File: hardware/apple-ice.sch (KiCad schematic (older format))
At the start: 80 parts, among them J1 TO_SP_DRIVE, J2 USB_B_Micro, J3 SPI_FLASH_PROG, P1 A2Bus-apple2, SW1 SW_Push, SW2 SW_Push, SW3 SW_Push, U1 SN74LVC8T245PW, U10 W25Q16JVSS, U2 SN74LVC8T245PW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

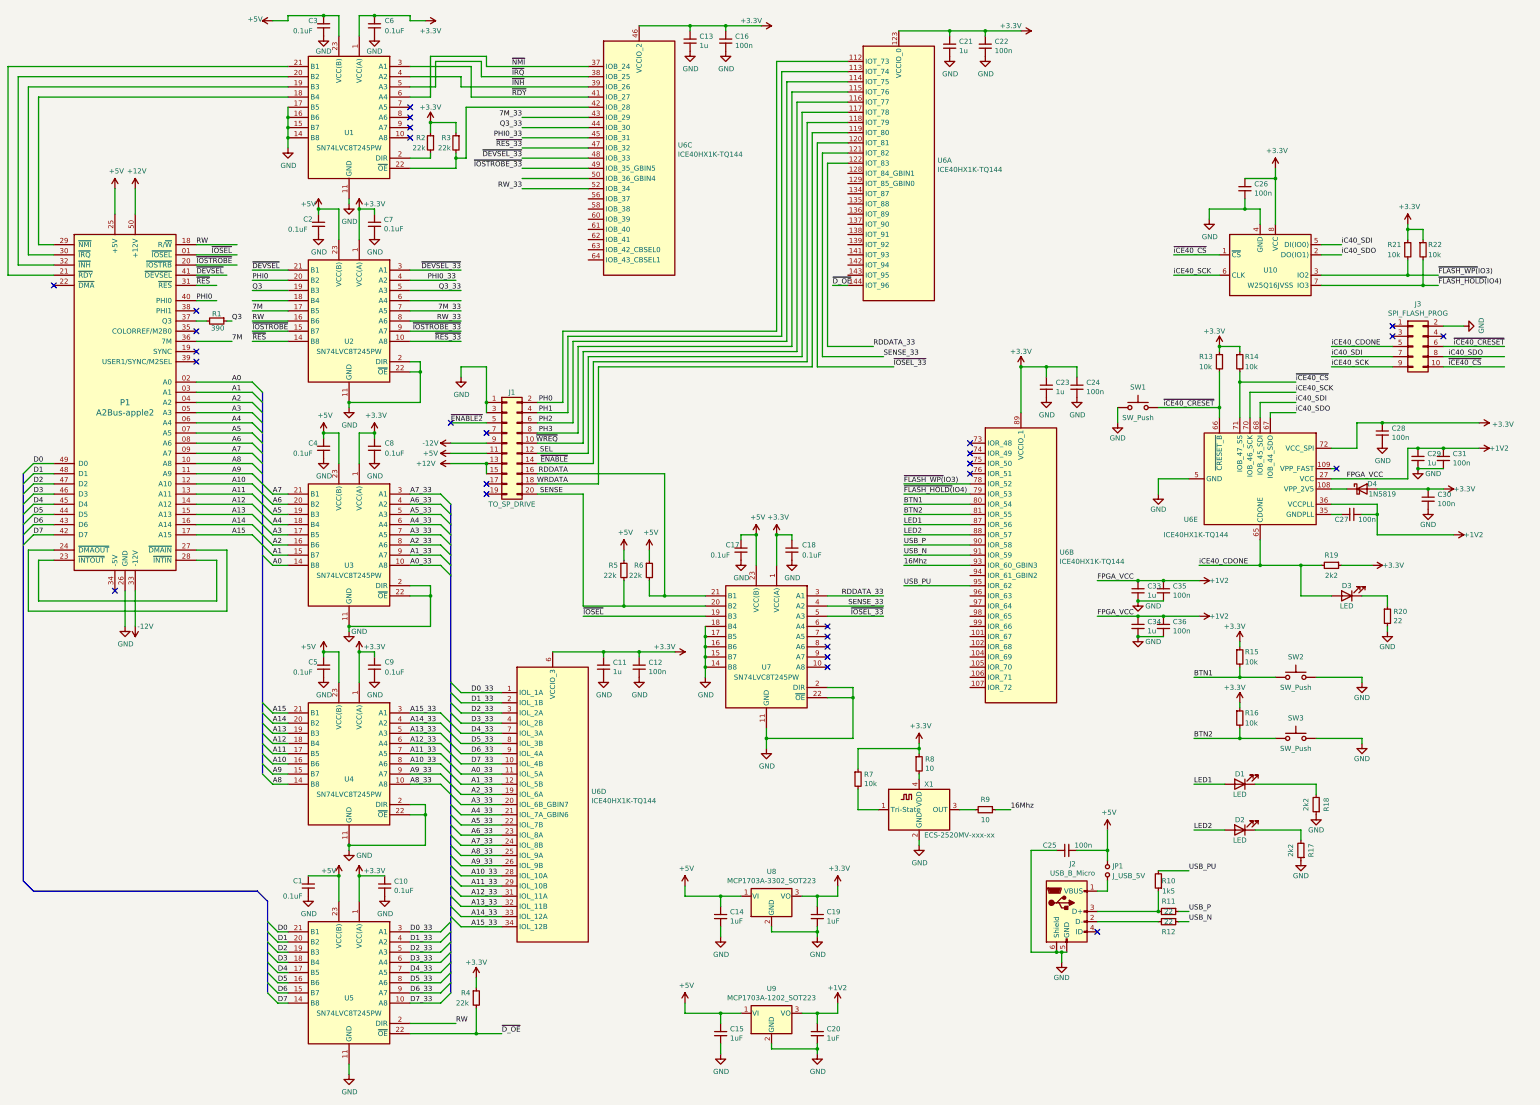
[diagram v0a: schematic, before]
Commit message: More routing, 80% finished
Signed-off-by: Rangel Ivanov <rangelivanov88@gmail.com>
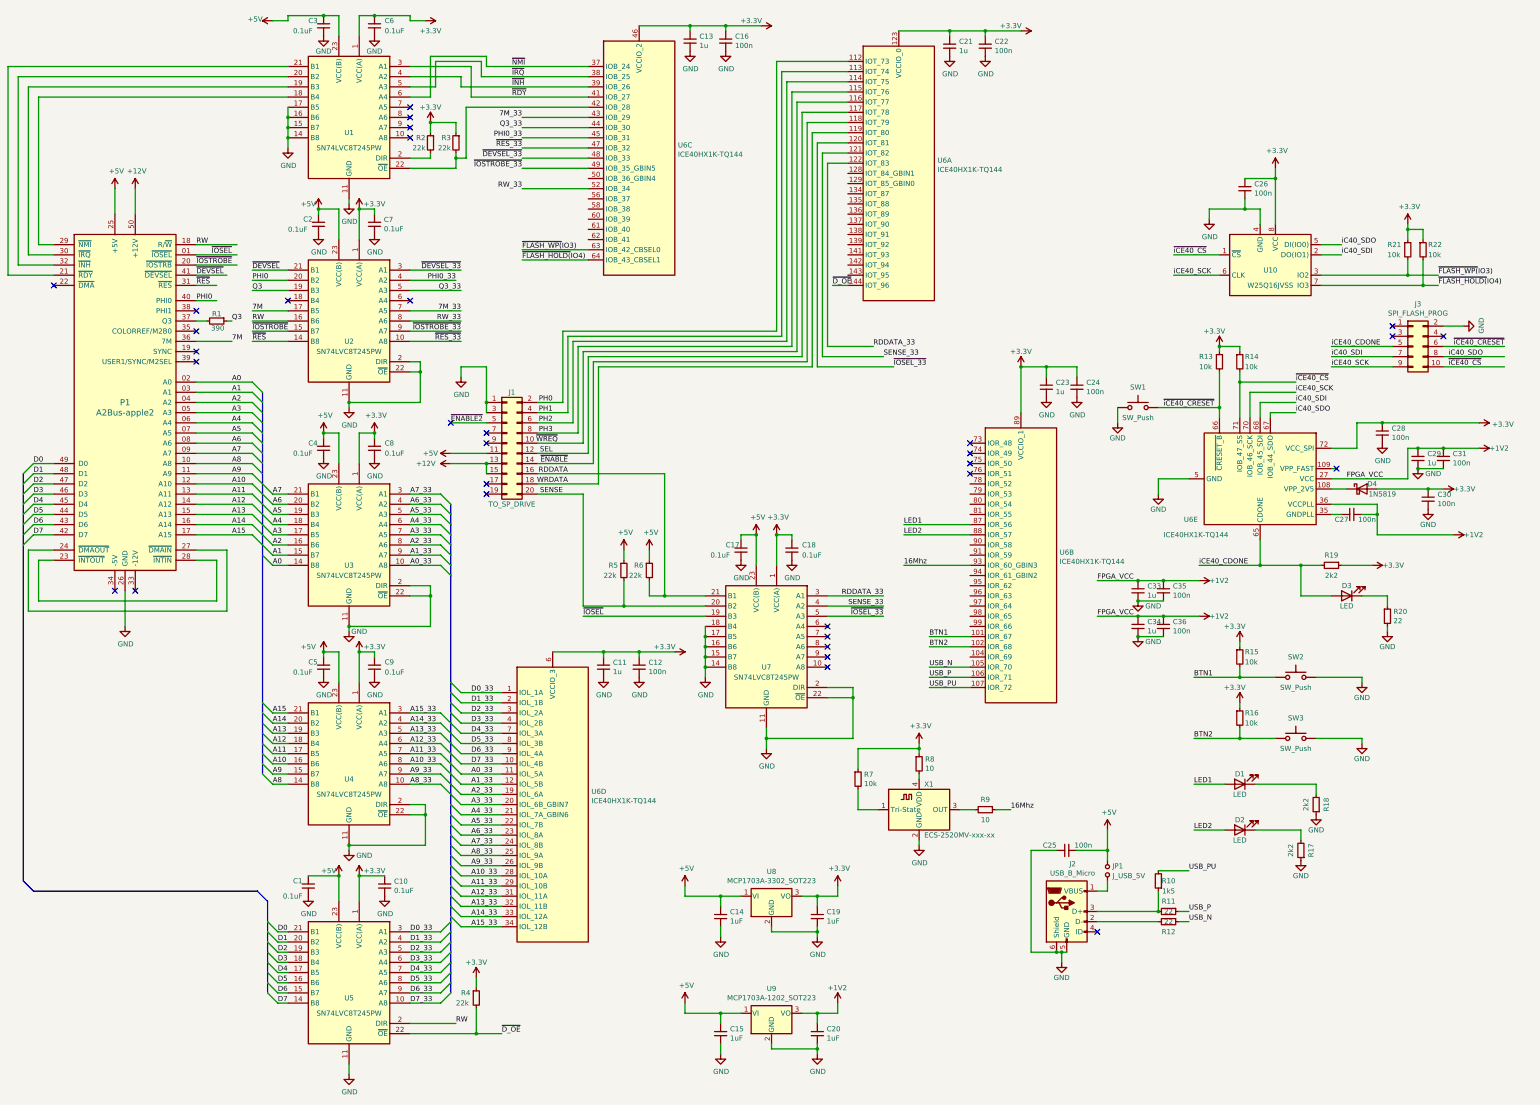
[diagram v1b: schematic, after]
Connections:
- net BTN1: now also U6.101 (IOR_67); no longer U6.80 (IOR_54)
- net BTN2: now also U6.102 (IOR_68); no longer U6.81 (IOR_55)
- net USB_N: now also U6.105 (IOR_70); no longer U6.91 (IOR_59)
- net USB_P: now also U6.106 (IOR_71); no longer U6.90 (IOR_58)
- net USB_PU: now also U6.107 (IOR_72); no longer U6.95 (IOR_62)
- net iC40_SDI: now also U10.2 (DO(IO1)); no longer U10.5 (DI(IO0))
- net iC40_SDO: now also U10.5 (DI(IO0)); no longer U10.2 (DO(IO1))
- net ~FLASH_HOLD(~IO4): now also U6.64 (IOB_43_CBSEL1); no longer U6.79 (IOR_53)
- net ~FLASH_WP(~IO3): now also U6.63 (IOB_42_CBSEL0); no longer U6.78 (IOR_52)
- net -12V: no longer names the net of J1.9 (Pin_9)
- net -12V: no longer P1.33 (-12V)
- no-connect marks 28 -> 32
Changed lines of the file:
@@
 Wire Wire Line
 	5850 4850 5500 4850
-Wire Wire Line
-	5850 4750 5500 4750
 NoConn ~ 5850 4650
 Text Label 5500 4550 0    50   ~ 0
@@
 Text Label 15200 3200 0    50   ~ 0
 ~FLASH_HOLD(~IO4)
-Text Label 9950 5150 0    50   ~ 0
-~FLASH_WP(~IO3)
-Wire Wire Line
-	9950 5150 10600 5150
-Text Label 9950 5250 0    50   ~ 0
+Text Label 6200 2950 0    50   ~ 0
 ~FLASH_HOLD(~IO4)
-Wire Wire Line
-	9950 5250 10600 5250
 Connection ~ 13050 4400
 Wire Wire Line
@@
 Wire Wire Line
 	14050 3200 15050 3200
+Text Label 14250 2800 0    50   ~ 0
+iC40_SDO
 Text Label 14250 2900 0    50   ~ 0
-iC40_SDO
-Text Label 14250 2800 0    50   ~ 0
 iC40_SDI
 Wire Wire Line
@@
 	6200 1750 6850 1750
 Wire Wire Line
-	5100 3350 5600 3350
-Wire Wire Line
 	6200 1850 6850 1850
 Wire Wire Line
@@
 Wire Wire Line
 	5100 3650 5600 3650
-Wire Wire Line
-	6200 2150 6850 2150
 Wire Wire Line
 	5100 3750 5600 3750
@@
 Wire Wire Line
 	2400 2250 2400 2500
-$Comp
-L apple-ice:-12V #PWR0160
-U 1 1 674F12EA
-P 2400 6550
-F 0 "#PWR0160" H 2400 6400 50  0001 C CNN
-F 1 "-12V" H 2300 6550 50  0000 C CNN
-F 2 "" H 2400 6550 50  0001 C CNN
-F 3 "" H 2400 6550 50  0001 C CNN
-	1    2400 6550
-	-1   0    0    1
-$EndComp
-Wire Wire Line
-	2400 6550 2400 6200
 NoConn ~ 2200 6200
 Wire Wire Line
@@
 	0    -1   -1   0
 $EndComp
-$Comp
-L apple-ice:-12V #PWR0169
-U 1 1 67831BCD
-P 5500 4750
-F 0 "#PWR0169" H 5500 4600 50  0001 C CNN
-F 1 "-12V" V 5500 4950 50  0000 C CNN
-F 2 "" H 5500 4750 50  0001 C CNN
-F 3 "" H 5500 4750 50  0001 C CNN
-	1    5500 4750
-	0    -1   -1   0
-$EndComp
 Wire Wire Line
 	7350 650  7850 650
@@
 	1    0    0    -1
 $EndComp
-Text Label 9950 5350 0    50   ~ 0
+Text Label 10200 6650 0    50   ~ 0
 BTN1
-Wire Wire Line
-	9950 5350 10600 5350
-Text Label 9950 5450 0    50   ~ 0
-BTN2
-Wire Wire Line
-	9950 5450 10600 5450
 $Comp
 L apple-ice:LED D1
@@
 USB_N
 NoConn ~ 11850 9550
-Text Label 9950 5750 0    50   ~ 0
+Text Label 10200 7050 0    50   ~ 0
 USB_P
-Wire Wire Line
-	9950 5750 10600 5750
-Text Label 9950 5850 0    50   ~ 0
+Text Label 10200 6950 0    50   ~ 0
 USB_N
-Wire Wire Line
-	9950 5850 10600 5850
-Text Label 9950 6150 0    50   ~ 0
+Text Label 10200 7150 0    50   ~ 0
 USB_PU
-Wire Wire Line
-	9950 6150 10600 6150
 $Comp
 L apple-ice:R_Small R10
@@
 Text Label 3550 3050 0    50   ~ 0
 ~DEVSEL
-Wire Wire Line
-	3550 3350 3900 3350
 Text Label 3550 3750 0    50   ~ 0
 ~RES
@@
 Wire Wire Line
 	9400 3200 9250 3200
+Text Label 6200 2850 0    50   ~ 0
+~FLASH_WP(~IO3)
+Wire Wire Line
+	6200 2950 6850 2950
+Wire Wire Line
+	6200 2850 6850 2850
+Wire Wire Line
+	10200 6950 10600 6950
+Wire Wire Line
+	10200 7050 10600 7050
+Wire Wire Line
+	10200 7150 10600 7150
+Wire Wire Line
+	10200 6650 10600 6650
+Text Label 10200 6750 0    50   ~ 0
+BTN2
+Wire Wire Line
+	10200 6750 10600 6750
+NoConn ~ 5850 4750
+NoConn ~ 3900 3350
+NoConn ~ 5100 3350
+NoConn ~ 2400 6200
 Wire Bus Line
 	3700 9250 3700 10150

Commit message: Finish routing
Signed-off-by: Rangel Ivanov <rangelivanov88@gmail.com>
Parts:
- added C?: 100n, apple-ice:C_0603_1608Metric_Pad1.08x0.95mm_HandSolder, symbol apple-ice:C_Small
- added C?: 1u, apple-ice:C_0603_1608Metric_Pad1.08x0.95mm_HandSolder, symbol apple-ice:C_Small
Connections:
- net +1V2: now also C?.1, C?.1
- net GND: now also C?.2, C?.2
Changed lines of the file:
@@
 NoConn ~ 5100 3350
 NoConn ~ 2400 6200
+$Comp
+L apple-ice:+1V2 #PWR?
+U 1 1 60FFB47A
+P 12850 6800
+F 0 "#PWR?" H 12850 6650 50  0001 C CNN
+F 1 "+1V2" V 12850 6900 50  0000 L CNN
+F 2 "" H 12850 6800 50  0001 C CNN
+F 3 "" H 12850 6800 50  0001 C CNN
+	1    12850 6800
+	0    1    1    0
+$EndComp
+$Comp
+L apple-ice:C_Small C?
+U 1 1 60FFB480
+P 12500 6900
+F 0 "C?" H 12592 6946 50  0000 L CNN
+F 1 "100n" H 12592 6855 50  0000 L CNN
+F 2 "apple-ice:C_0603_1608Metric_Pad1.08x0.95mm_HandSolder" H 12500 6900 50  0001 C CNN
+F 3 "~" H 12500 6900 50  0001 C CNN
+	1    12500 6900
+	1    0    0    -1
+$EndComp
+Connection ~ 12500 6800
+$Comp
+L apple-ice:C_Small C?
+U 1 1 60FFB487
+P 12250 6900
+F 0 "C?" H 12342 6946 50  0000 L CNN
+F 1 "1u" H 12342 6855 50  0000 L CNN
+F 2 "apple-ice:C_0603_1608Metric_Pad1.08x0.95mm_HandSolder" H 12250 6900 50  0001 C CNN
+F 3 "~" H 12250 6900 50  0001 C CNN
+	1    12250 6900
+	1    0    0    -1
+$EndComp
+Connection ~ 12250 6800
+Wire Wire Line
+	12250 6800 12500 6800
+$Comp
+L apple-ice:GND #PWR?
+U 1 1 60FFB48F
+P 12250 7000
+F 0 "#PWR?" H 12250 6750 50  0001 C CNN
+F 1 "GND" H 12400 6950 50  0000 C CNN
+F 2 "" H 12250 7000 50  0001 C CNN
+F 3 "" H 12250 7000 50  0001 C CNN
+	1    12250 7000
+	1    0    0    -1
+$EndComp
+Wire Wire Line
+	12500 7000 12250 7000
+Connection ~ 12250 7000
+Wire Wire Line
+	12500 6800 12850 6800
+Text Label 11850 6800 0    50   ~ 0
+FPGA_VCC
+Wire Wire Line
+	11850 6800 12250 6800
 Wire Bus Line
 	3700 9250 3700 10150

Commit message: Add 2x15 pin header
Signed-off-by: Rangel Ivanov <rangelivanov88@gmail.com>
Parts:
- added J4: Conn_02x15_Odd_Even, symbol apple-ice:Conn_02x15_Odd_Even
- gave numbers to parts that had none: 2
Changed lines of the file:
@@
 NoConn ~ 2400 6200
 $Comp
-L apple-ice:+1V2 #PWR?
+L apple-ice:+1V2 #PWR06
 U 1 1 60FFB47A
 P 12850 6800
-F 0 "#PWR?" H 12850 6650 50  0001 C CNN
+F 0 "#PWR06" H 12850 6650 50  0001 C CNN
 F 1 "+1V2" V 12850 6900 50  0000 L CNN
 F 2 "" H 12850 6800 50  0001 C CNN
@@
 $EndComp
 $Comp
-L apple-ice:C_Small C?
+L apple-ice:C_Small C37
 U 1 1 60FFB480
 P 12500 6900
-F 0 "C?" H 12592 6946 50  0000 L CNN
+F 0 "C37" H 12592 6946 50  0000 L CNN
 F 1 "100n" H 12592 6855 50  0000 L CNN
 F 2 "apple-ice:C_0603_1608Metric_Pad1.08x0.95mm_HandSolder" H 12500 6900 50  0001 C CNN
@@
 Connection ~ 12500 6800
 $Comp
-L apple-ice:C_Small C?
+L apple-ice:C_Small C32
 U 1 1 60FFB487
 P 12250 6900
-F 0 "C?" H 12342 6946 50  0000 L CNN
+F 0 "C32" H 12342 6946 50  0000 L CNN
 F 1 "1u" H 12342 6855 50  0000 L CNN
 F 2 "apple-ice:C_0603_1608Metric_Pad1.08x0.95mm_HandSolder" H 12250 6900 50  0001 C CNN
@@
 	12250 6800 12500 6800
 $Comp
-L apple-ice:GND #PWR?
+L apple-ice:GND #PWR05
 U 1 1 60FFB48F
 P 12250 7000
-F 0 "#PWR?" H 12250 6750 50  0001 C CNN
+F 0 "#PWR05" H 12250 6750 50  0001 C CNN
 F 1 "GND" H 12400 6950 50  0000 C CNN
 F 2 "" H 12250 7000 50  0001 C CNN
@@
 Wire Bus Line
 	3650 4250 3650 8000
+$Comp
+L apple-ice:Conn_02x15_Odd_Even J4
+U 1 1 60FC5A6A
+P 12300 1550
+F 0 "J4" H 12350 2467 50  0000 C CNN
+F 1 "Conn_02x15_Odd_Even" H 12350 2376 50  0000 C CNN
+F 2 "" H 12300 1550 50  0001 C CNN
+F 3 "~" H 12300 1550 50  0001 C CNN
+	1    12300 1550
+	1    0    0    -1
+$EndComp
 $EndSCHEMATC

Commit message: Route double pmod header
Signed-off-by: Rangel Ivanov <rangelivanov88@gmail.com>
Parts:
- J4: footprint (none) -> apple-ice:PinSocket_2x15_P2.54mm_Horizontal
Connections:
- net +3.3V: now also J4.1 (Pin_1), J4.19 (Pin_19), J4.2 (Pin_2), J4.20 (Pin_20)
- net GND: now also J4.21 (Pin_21), J4.22 (Pin_22), J4.3 (Pin_3), J4.4 (Pin_4)
- net PMOD_0: now reaches U6.73 (IOR_48)
- net PMOD_0: now also J4.5 (Pin_5)
- net PMOD_1: now reaches U6.74 (IOR_49)
- net PMOD_1: now also J4.6 (Pin_6)
- net PMOD_2: now reaches U6.75 (IOR_50)
- net PMOD_2: now also J4.7 (Pin_7)
- net PMOD_3: now reaches U6.76 (IOR_51)
- net PMOD_3: now also J4.8 (Pin_8)
- net PMOD_4: now reaches U6.78 (IOR_52)
- net PMOD_4: now also J4.9 (Pin_9)
- net PMOD_5: now reaches U6.79 (IOR_53)
- net PMOD_5: now also J4.10 (Pin_10)
- net PMOD_6: now reaches U6.80 (IOR_54)
- net PMOD_6: now also J4.11 (Pin_11)
- net PMOD_7: now reaches U6.81 (IOR_55)
- net PMOD_7: now also J4.12 (Pin_12)
- net PMOD1_0: now reaches U6.90 (IOR_58)
- net PMOD1_0: now also J4.23 (Pin_23)
- net PMOD1_1: now reaches U6.91 (IOR_59)
- net PMOD1_1: now also J4.24 (Pin_24)
- net PMOD1_2: now reaches U6.94 (IOR_61_GBIN2)
- net PMOD1_2: now also J4.25 (Pin_25)
- net PMOD1_3: now reaches U6.95 (IOR_62)
- net PMOD1_3: now also J4.26 (Pin_26)
- net PMOD1_4: now reaches U6.96 (IOR_63)
- net PMOD1_4: now also J4.27 (Pin_27)
- net PMOD1_5: now reaches U6.97 (IOR_64)
- net PMOD1_5: now also J4.28 (Pin_28)
- net PMOD1_6: now reaches U6.98 (IOR_65)
- net PMOD1_6: now also J4.29 (Pin_29)
- net PMOD1_7: now reaches U6.99 (IOR_66)
- net PMOD1_7: now also J4.30 (Pin_30)
- no-connect marks 32 -> 34

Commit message: Add 5, 12 and -12 power rails to pmod connection
Signed-off-by: Rangel Ivanov <rangelivanov88@gmail.com>
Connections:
- net +12V: now also J4.17 (Pin_17)
- net +5V: now also J4.13 (Pin_13)
- net GND: now also J4.14 (Pin_14), J4.16 (Pin_16), J4.18 (Pin_18)
- net -12V: now reaches J4.15 (Pin_15)
- net -12V: now also P1.33 (-12V)
- no-connect marks 34 -> 46
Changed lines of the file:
@@
 	1    0    0    -1
 $EndComp
-$Comp
-L apple-ice:GND #PWR0110
-U 1 1 61314AF4
-P 4500 10950
-F 0 "#PWR0110" H 4500 10700 50  0001 C CNN
-F 1 "GND" H 4505 10777 50  0000 C CNN
-F 2 "" H 4500 10950 50  0001 C CNN
-F 3 "" H 4500 10950 50  0001 C CNN
-	1    4500 10950
-	1    0    0    -1
-$EndComp
 Wire Wire Line
 	4500 10850 4500 10950
@@
 Wire Wire Line
 	2400 2250 2400 2500
-NoConn ~ 2200 6200
 Wire Wire Line
 	2300 6200 2300 6550
@@
 NoConn ~ 3900 3350
 NoConn ~ 5100 3350
-NoConn ~ 2400 6200
 $Comp
 L apple-ice:+1V2 #PWR06
@@
 	11850 6800 12250 6800
 $Comp
-L apple-ice:Conn_02x15_Odd_Even J4
-U 1 1 60FC5A6A
-P 12300 1550
-F 0 "J4" H 12350 550 50  0000 C CNN
-F 1 "Conn_02x15_Odd_Even" H 12350 650 50  0000 C CNN
-F 2 "apple-ice:PinSocket_2x15_P2.54mm_Horizontal" H 12300 1550 50  0001 C CNN
-F 3 "~" H 12300 1550 50  0001 C CNN
-	1    12300 1550
-	1    0    0    1
-$EndComp
-$Comp
 L apple-ice:+3.3V #PWR0160
 U 1 1 6129C23F
@@
 	1    0    0    -1
 $EndComp
-NoConn ~ 12100 1450
-NoConn ~ 12100 1550
-NoConn ~ 12100 1650
-NoConn ~ 12600 1650
-NoConn ~ 12600 1550
-NoConn ~ 12600 1450
 Wire Wire Line
 	10600 5450 9950 5450
@@
 Wire Wire Line
 	12600 1150 12950 1150
-Wire Bus Line
-	3700 9250 3700 10150
-Wire Bus Line
-	1300 5050 1300 9050
-Wire Bus Line
-	5500 5350 5500 10150
-Wire Bus Line
-	3650 4250 3650 8000
 Text Label 12600 1150 0    50   ~ 0
 PMOD1_1
-Text Label 12050 950  2    50   ~ 0
+Text Label 12100 950  2    50   ~ 0
 PMOD1_4
 Text Label 12950 950  2    50   ~ 0
@@
 Text Label 12600 1050 0    50   ~ 0
 PMOD1_3
+NoConn ~ 10600 6850
+NoConn ~ 9400 2100
+NoConn ~ 9400 2200
+NoConn ~ 9400 2300
+NoConn ~ 9400 2400
+NoConn ~ 9400 2500
+NoConn ~ 9400 2600
+NoConn ~ 9400 2700
+NoConn ~ 9400 2800
+NoConn ~ 9400 2900
+NoConn ~ 9400 3000
+NoConn ~ 9400 3100
+NoConn ~ 6850 2150
+NoConn ~ 6850 2350
+NoConn ~ 6850 2450
+NoConn ~ 6850 2550
+NoConn ~ 6850 2650
+NoConn ~ 6850 2750
+$Comp
+L apple-ice:GND #PWR0110
+U 1 1 6206DFB6
+P 4500 10950
+F 0 "#PWR0110" H 4500 10700 50  0001 C CNN
+F 1 "GND" H 4650 10900 50  0000 C CNN
+F 2 "" H 4500 10950 50  0001 C CNN
+F 3 "" H 4500 10950 50  0001 C CNN
+	1    4500 10950
+	1    0    0    -1
+$EndComp
+NoConn ~ 9900 2750
+Wire Wire Line
+	2400 6200 2400 6550
+Wire Wire Line
+	2400 6550 2550 6550
+Wire Wire Line
+	2550 6550 2550 6750
+$Comp
+L apple-ice:-12V #PWR0197
+U 1 1 6223392F
+P 2550 6750
+F 0 "#PWR0197" H 2550 6600 50  0001 C CNN
+F 1 "-12V" H 2565 6923 50  0000 C CNN
+F 2 "" H 2550 6750 50  0001 C CNN
+F 3 "" H 2550 6750 50  0001 C CNN
+	1    2550 6750
+	-1   0    0    1
+$EndComp
+$Comp
+L apple-ice:Conn_02x15_Odd_Even J4
+U 1 1 60FC5A6A
+P 12300 1550
+F 0 "J4" H 12350 550 50  0000 C CNN
+F 1 "Conn_02x15_Odd_Even" H 12350 650 50  0000 C CNN
+F 2 "apple-ice:PinSocket_2x15_P2.54mm_Horizontal" H 12300 1550 50  0001 C CNN
+F 3 "~" H 12300 1550 50  0001 C CNN
+	1    12300 1550
+	1    0    0    1
+$EndComp
+$Comp
+L apple-ice:-12V #PWR0198
+U 1 1 623E12E9
+P 11100 1350
+F 0 "#PWR0198" H 11100 1200 50  0001 C CNN
+F 1 "-12V" H 11100 1500 50  0000 C CNN
+F 2 "" H 11100 1350 50  0001 C CNN
+F 3 "" H 11100 1350 50  0001 C CNN
+	1    11100 1350
+	1    0    0    -1
+$EndComp
+$Comp
+L apple-ice:+12V #PWR0199
+U 1 1 624447F8
+P 11250 1350
+F 0 "#PWR0199" H 11250 1200 50  0001 C CNN
+F 1 "+12V" H 11350 1500 50  0000 C CNN
+F 2 "" H 11250 1350 50  0001 C CNN
+F 3 "" H 11250 1350 50  0001 C CNN
+	1    11250 1350
+	1    0    0    -1
+$EndComp
+$Comp
+L apple-ice:+5V #PWR0200
+U 1 1 624A93D5
+P 10950 1350
+F 0 "#PWR0200" H 10950 1200 50  0001 C CNN
+F 1 "+5V" H 10850 1500 50  0000 C CNN
+F 2 "" H 10950 1350 50  0001 C CNN
+F 3 "" H 10950 1350 50  0001 C CNN
+	1    10950 1350
+	1    0    0    -1
+$EndComp
+NoConn ~ 2200 6200
+Wire Wire Line
+	11250 1450 11250 1350
+Wire Wire Line
+	11250 1450 12100 1450
+Wire Wire Line
+	12100 1550 11100 1550
+Wire Wire Line
+	11100 1550 11100 1350
+Wire Wire Line
+	12100 1650 10950 1650
+Wire Wire Line
+	10950 1650 10950 1350
+Wire Wire Line
+	12600 1450 12600 1550
+Wire Wire Line
+	12600 1650 12600 1550
+Connection ~ 12600 1550
+Wire Wire Line
+	12600 1450 13300 1450
+Wire Bus Line
+	3700 9250 3700 10150
+Wire Bus Line
+	1300 5050 1300 9050
+Wire Bus Line
+	5500 5350 5500 10150
+Wire Bus Line
+	3650 4250 3650 8000
+Connection ~ 12600 1450
+Connection ~ 13300 1450
 $EndSCHEMATC

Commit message: Move io_strobe signal to an FPGA pin that is not shared with the PLL
Signed-off-by: Rangel Ivanov <rangelivanov88@gmail.com>
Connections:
- net ~IOSTROBE_33: now also U6.56 (IOB_37); no longer U6.49 (IOB_35_GBIN5)
- no-connect marks 46 -> 45
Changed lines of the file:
@@
 	5100 3550 5600 3550
-Wire Wire Line
-	6200 2050 6850 2050
 Wire Wire Line
 	5100 3650 5600 3650
@@
 Text Label 9750 6450 2    50   ~ 0
 ~IOSEL_33
-Text Label 6200 2050 2    50   ~ 0
+Text Label 6200 2350 2    50   ~ 0
 ~IOSTROBE_33
 Text Label 6200 1950 2    50   ~ 0
@@
 NoConn ~ 9400 3100
 NoConn ~ 6850 2150
-NoConn ~ 6850 2350
 NoConn ~ 6850 2450
 NoConn ~ 6850 2550
@@
 Wire Wire Line
 	12600 1450 13300 1450
+Connection ~ 12600 1450
+Connection ~ 13300 1450
+Wire Wire Line
+	6200 2350 6850 2350
 Wire Bus Line
 	3700 9250 3700 10150
@@
 Wire Bus Line
 	3650 4250 3650 8000
-Connection ~ 12600 1450
-Connection ~ 13300 1450
 $EndSCHEMATC
